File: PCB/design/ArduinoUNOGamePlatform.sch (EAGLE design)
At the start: 23 parts, among them J3 PJ-320D-A, Q1 ON_SEMICONDUCTOR_BC849BLT1GON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, Q2 ON_SEMICONDUCTOR_BC849BLT1GON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

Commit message: Fixed some stale comments and removed commented out old code. Changed some resistor values on PCB following testing. Added designation to move order number under the NES port if using JLC to produce board. Also changed pinouts for buttons to match buttons on shield (I had reversed the positions on PORTC!
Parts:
- R1: value DNP -> 75R
- R2: value 180R -> 220R
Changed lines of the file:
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@@
 <part name="U$2" library="adafruit" library_urn="urn:adsk.eagle:library:21079626" deviceset="ARDUINO" device="-BPLACE" package3d_urn="urn:adsk.eagle:package:21080989/1"/>
 <part name="Q2" library="On Semiconductor - BC849BLT1G" library_urn="urn:adsk.eagle:library:22357129" deviceset="ON_SEMICONDUCTOR_BC849BLT1G" device="ON_SEMICONDUCTOR_BC849BLT1G_0_0" package3d_urn="urn:adsk.eagle:package:22357132/2"/>
-<part name="R2" library="ESP32_DMX_Audio" library_urn="urn:adsk.eagle:library:21091620" deviceset="52101-101-REV-A_RC-MASTER-SMD_R_" device="0603MP" package3d_urn="urn:adsk.eagle:package:21091780/2" value="180R"/>
+<part name="R2" library="ESP32_DMX_Audio" library_urn="urn:adsk.eagle:library:21091620" deviceset="52101-101-REV-A_RC-MASTER-SMD_R_" device="0603MP" package3d_urn="urn:adsk.eagle:package:21091780/2" value="220R"/>
 <part name="R3" library="ESP32_DMX_Audio" library_urn="urn:adsk.eagle:library:21091620" deviceset="52101-101-REV-A_RC-MASTER-SMD_R_" device="0603MP" package3d_urn="urn:adsk.eagle:package:21091780/2" value="1K2"/>
 <part name="R8" library="ESP32_DMX_Audio" library_urn="urn:adsk.eagle:library:21091620" deviceset="52101-101-REV-A_RC-MASTER-SMD_R_" device="0603MP" package3d_urn="urn:adsk.eagle:package:21091780/2" value="470R"/>
@@
 <part name="B8" library="K2-1107ST-A4SW-06" library_urn="urn:adsk.eagle:library:30827574" deviceset="K2-1107ST-A4SW-06" device="" package3d_urn="urn:adsk.eagle:package:30827578/3"/>
 <part name="GND14" library="supply1" library_urn="urn:adsk.eagle:library:371" deviceset="GND" device=""/>
-<part name="R1" library="ESP32_DMX_Audio" library_urn="urn:adsk.eagle:library:21091620" deviceset="52101-101-REV-A_RC-MASTER-SMD_R_" device="0603MP" package3d_urn="urn:adsk.eagle:package:21091780/2" value="DNP"/>
+<part name="R1" library="ESP32_DMX_Audio" library_urn="urn:adsk.eagle:library:21091620" deviceset="52101-101-REV-A_RC-MASTER-SMD_R_" device="0603MP" package3d_urn="urn:adsk.eagle:package:21091780/2" value="75R"/>
 <part name="GND15" library="supply1" library_urn="urn:adsk.eagle:library:371" deviceset="GND" device=""/>
 <part name="U$3" library="PJ-320D-A" library_urn="urn:adsk.eagle:library:43570733" deviceset="NES-CONTROLLER-PORT" device="" package3d_urn="urn:adsk.eagle:package:43570976/2"/>

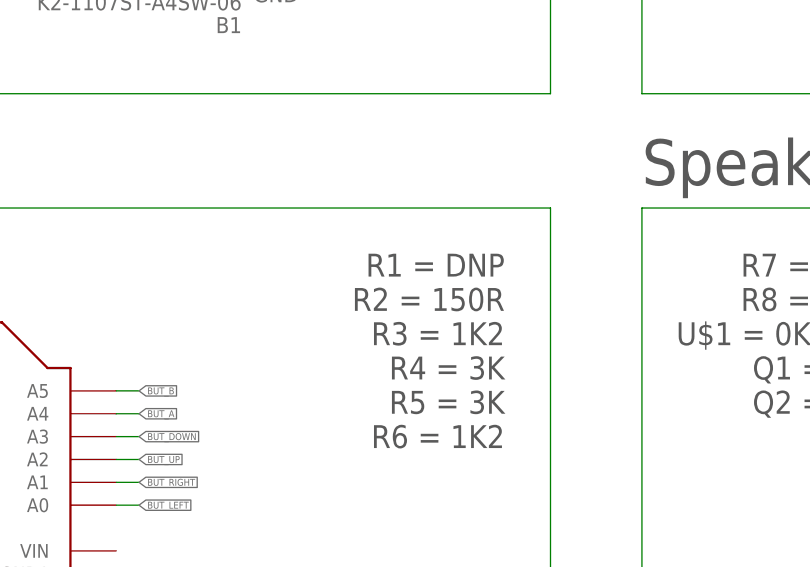
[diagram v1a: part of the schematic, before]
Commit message: Updated schematic to match design files
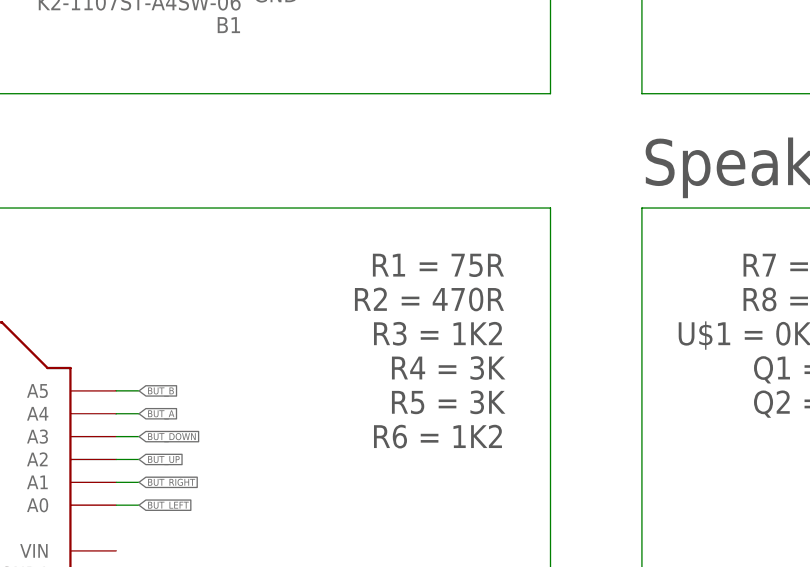
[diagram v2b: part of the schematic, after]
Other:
- note added: "R1 = 75R R2 = 470R R3 = 1K2 R4 = 3K R5 = 3K R6 = 1K2"
- note removed: "R1 = DNP R2 = 150R R3 = 1K2 R4 = 3K R5 = 3K R6 = 1K2"
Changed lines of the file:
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@@
 <text x="256.54" y="205.74" size="5.08" layer="97">NES Controller</text>
 <text x="256.54" y="144.78" size="5.08" layer="97">Speaker output (optional)</text>
-<text x="241.3" y="137.16" size="2.54" layer="97" rot="R180">R1 = DNP
-R2 = 150R
+<text x="241.3" y="137.16" size="2.54" layer="97" rot="R180">R1 = 75R
+R2 = 470R
 R3 = 1K2
 R4 = 3K

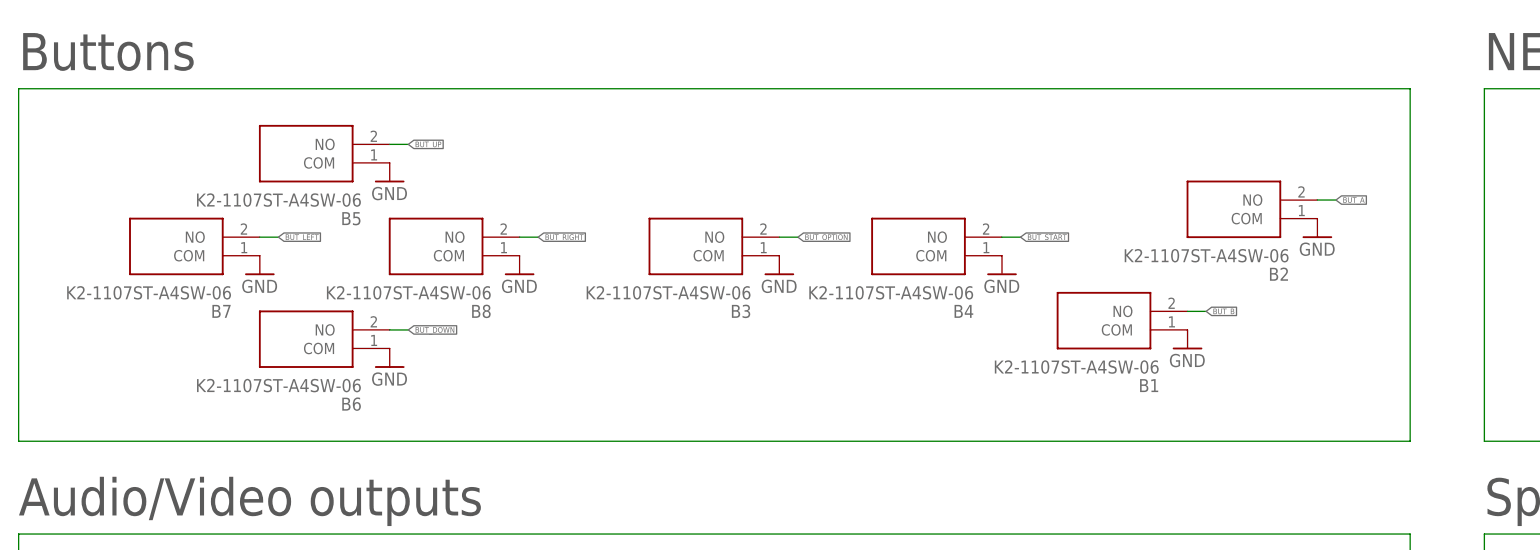
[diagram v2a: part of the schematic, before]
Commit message: Modified PCB design to make it easier for hand-soldering, and also changed to better buttons
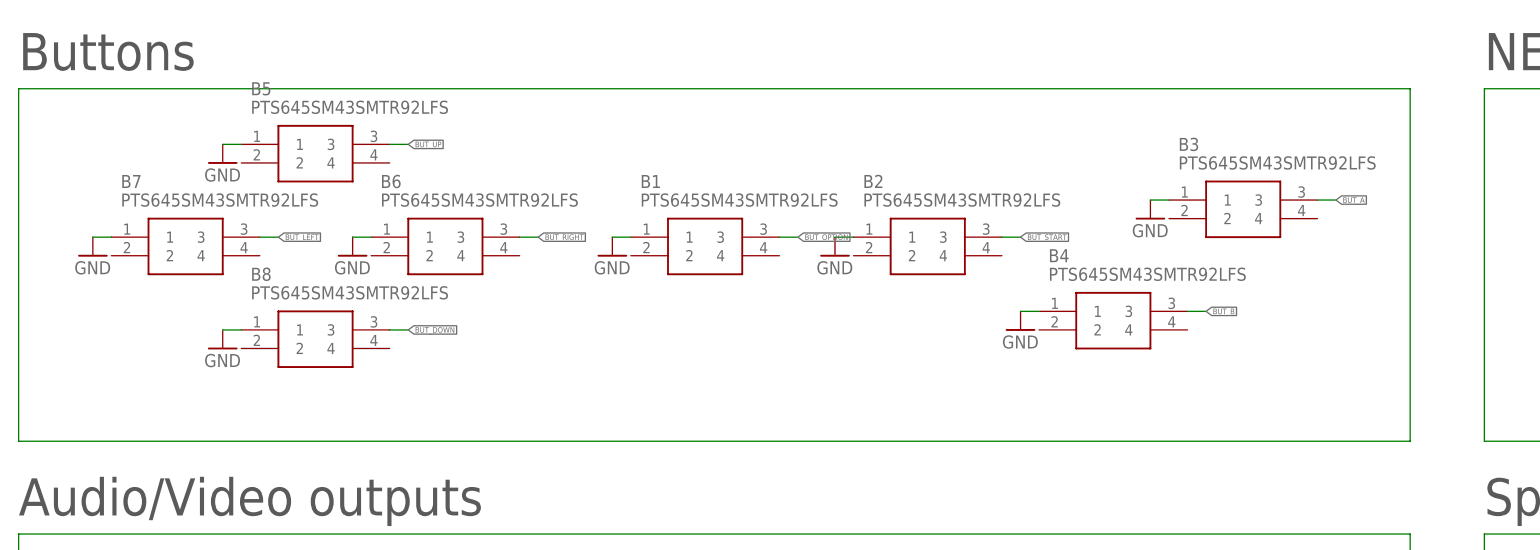
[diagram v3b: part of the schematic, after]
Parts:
- B1, B2, B3, B4, B5, B6, B7, B8: value K2-1107ST-A4SW-06 -> PTS645SM43SMTR92LFS; device K2-1107ST-A4SW-06:K2-1107ST-A4SW-06 -> PTS645SM43SMTR92LFS:PTS645SM43SMTR92LFS
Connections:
- net BUT_A: now also B3.3; no longer B2.NO
- net BUT_B: now also B4.3; no longer B1.NO
- net BUT_DOWN: now also B8.3; no longer B6.NO
- net BUT_LEFT: now also B7.3; no longer B7.NO
- net BUT_OPTION: now also B1.3; no longer B3.NO
- net BUT_RIGHT: now also B6.3; no longer B8.NO
- net BUT_START: now also B2.3; no longer B4.NO
- net BUT_UP: now also B5.3; no longer B5.NO
- net GND: now also B1.1, B2.1, B3.1, B4.1, B5.1, B6.1, B7.1, B8.1; no longer B1.COM, B2.COM, B3.COM, B4.COM, B5.COM, B6.COM, B7.COM, B8.COM

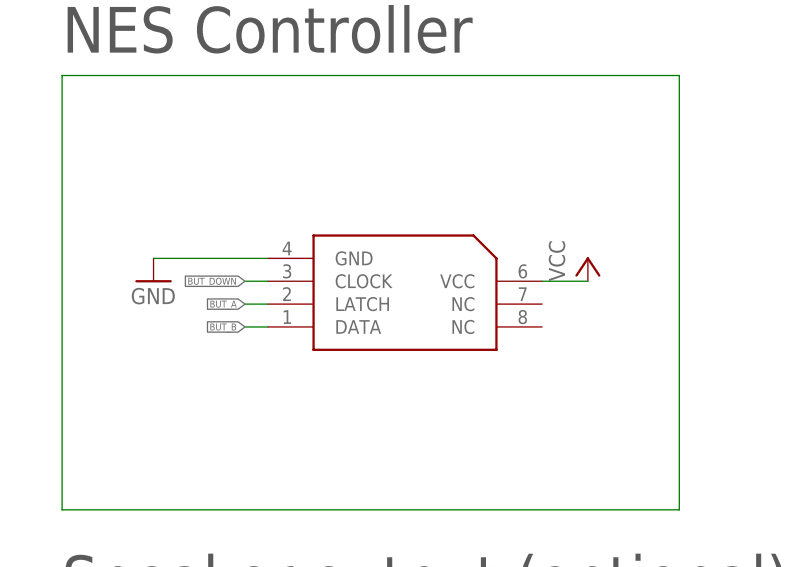
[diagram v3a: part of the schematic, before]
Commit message: Updated PCB design to modify NES port part. Holes were too tight and not enough clearance for it under board, so now on top. Also pins moved slightly further apart to make soldering a little easier
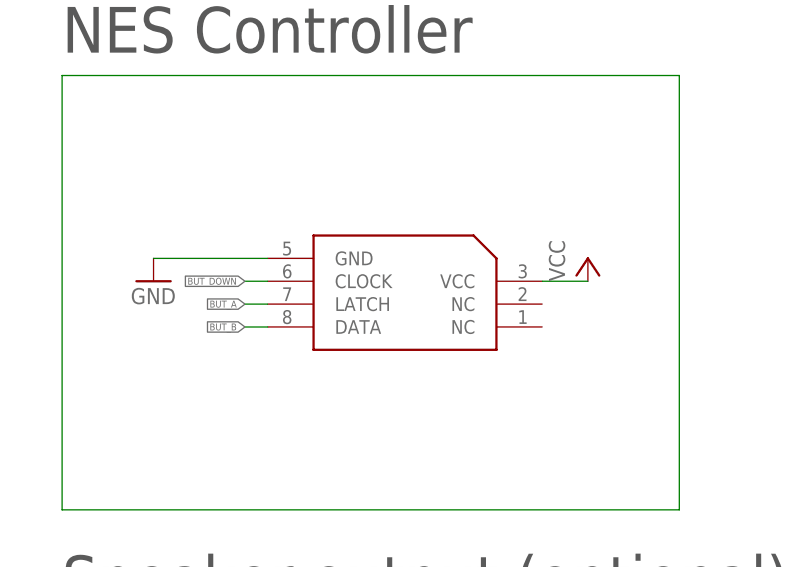
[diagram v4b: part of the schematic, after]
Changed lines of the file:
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@@
 <part name="R1" library="ESP32_DMX_Audio" library_urn="urn:adsk.eagle:library:21091620" deviceset="52101-101-REV-A_RC-MASTER-SMD_R_" device="0603MP" package3d_urn="urn:adsk.eagle:package:21091780/2" value="75R"/>
 <part name="GND15" library="supply1" library_urn="urn:adsk.eagle:library:371" deviceset="GND" device=""/>
-<part name="U$3" library="PJ-320D-A" library_urn="urn:adsk.eagle:library:43570733" deviceset="NES-CONTROLLER-PORT" device="" package3d_urn="urn:adsk.eagle:package:43570976/2"/>
+<part name="U$3" library="PJ-320D-A" library_urn="urn:adsk.eagle:library:43570733" deviceset="NES-CONTROLLER-PORT" device="" package3d_urn="urn:adsk.eagle:package:43570976/3"/>
 <part name="GND16" library="supply1" library_urn="urn:adsk.eagle:library:371" deviceset="GND" device=""/>
 <part name="P+3" library="supply1" library_urn="urn:adsk.eagle:library:371" deviceset="VCC" device=""/>

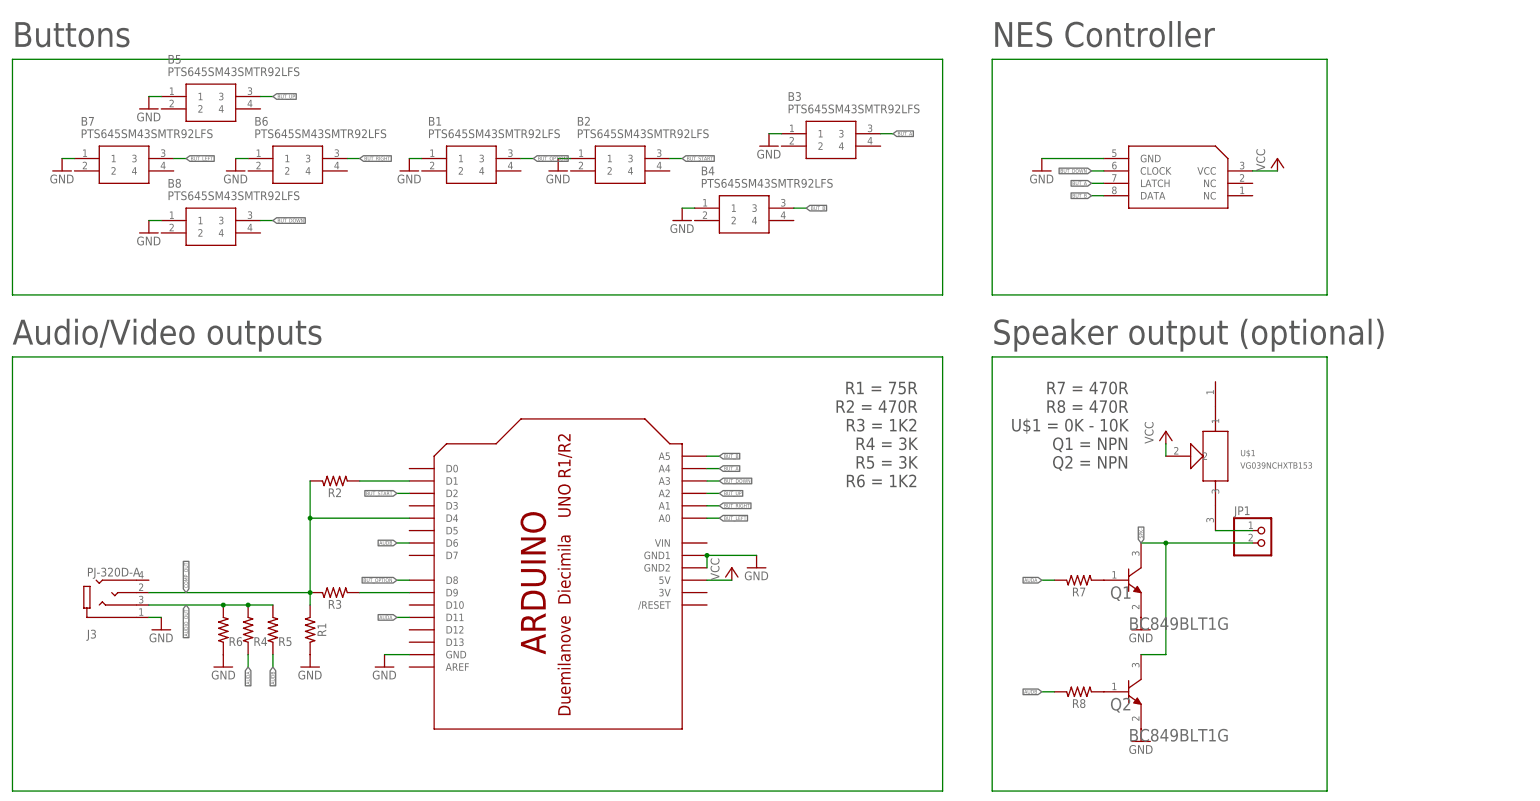
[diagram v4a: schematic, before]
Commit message: Decided to move the pins used for the controller to unused pins on PORTB so that buttons could be used in addition, in future games. Also modified input a little to controller reading. New PCB images and schematic
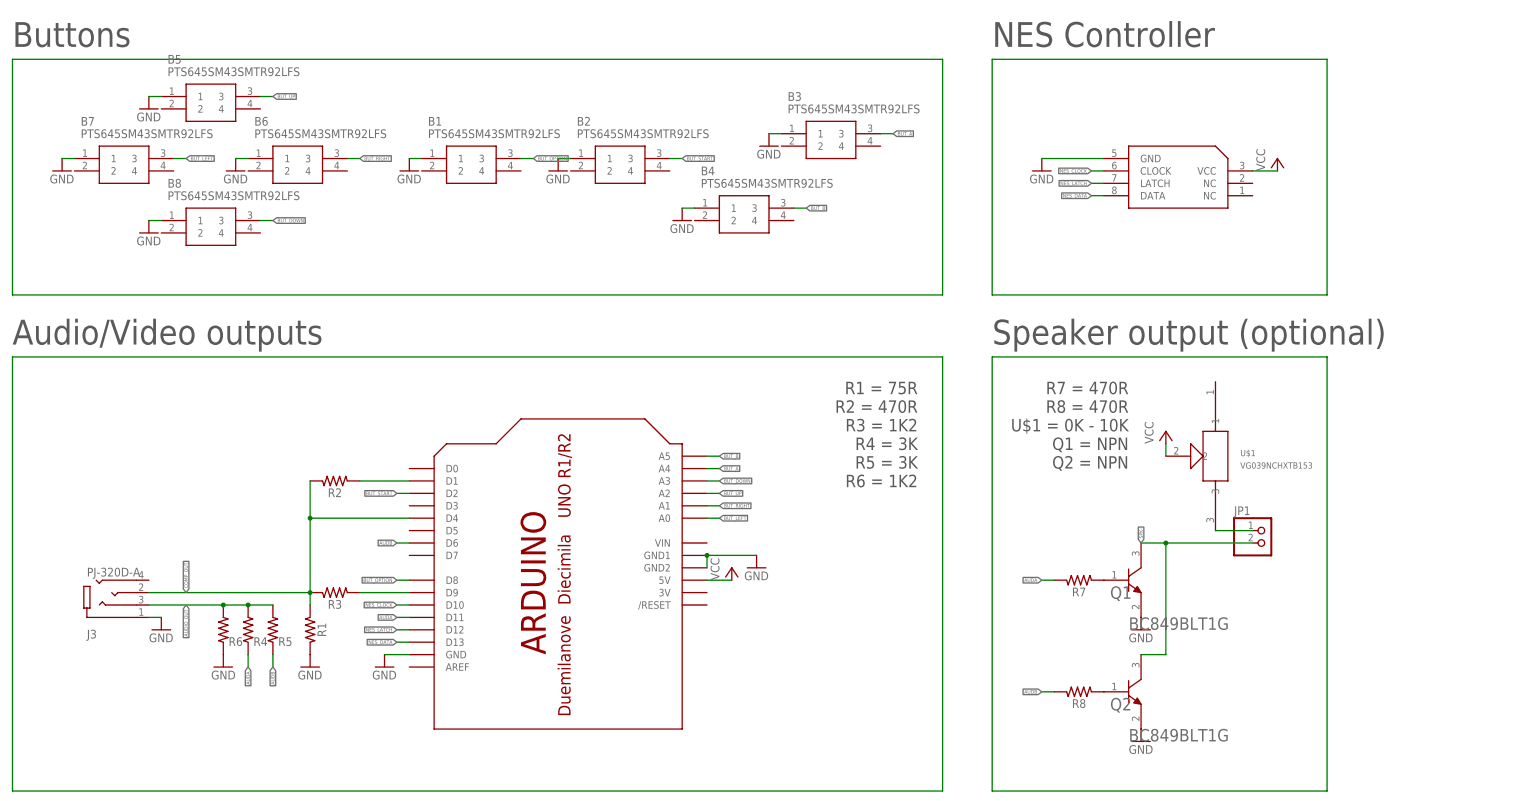
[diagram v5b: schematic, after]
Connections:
- new net NES_CLOCK: U$2.D10, U$3.CLOCK
- new net NES_DATA: U$2.D13, U$3.DATA
- new net NES_LATCH: U$2.D12, U$3.LATCH
- net BUT_A: no longer U$3.LATCH
- net BUT_B: no longer U$3.DATA
- net BUT_DOWN: no longer U$3.CLOCK
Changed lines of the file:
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@@
 <pinref part="B4" gate="G$1" pin="3"/>
-</segment>
-<segment>
-<wire x1="276.86" y1="175.26" x2="279.4" y2="175.26" width="0.1524" layer="91"/>
-<label x="276.86" y="175.26" size="0.762" layer="95" rot="R180" xref="yes"/>
-<pinref part="U$3" gate="G$1" pin="DATA"/>
 </segment>
 </net>
@@
 <pinref part="B3" gate="G$1" pin="3"/>
 </segment>
-<segment>
-<wire x1="276.86" y1="177.8" x2="279.4" y2="177.8" width="0.1524" layer="91"/>
-<label x="276.86" y="177.8" size="0.762" layer="95" rot="R180" xref="yes"/>
-<pinref part="U$3" gate="G$1" pin="LATCH"/>
-</segment>
 </net>
 <net name="BUT_DOWN" class="0">
@@
 <label x="109.22" y="170.18" size="0.762" layer="95" xref="yes"/>
 <pinref part="B8" gate="G$1" pin="3"/>
-</segment>
-<segment>
-<wire x1="276.86" y1="180.34" x2="279.4" y2="180.34" width="0.1524" layer="91"/>
-<label x="276.86" y="180.34" size="0.762" layer="95" rot="R180" xref="yes"/>
-<pinref part="U$3" gate="G$1" pin="CLOCK"/>
 </segment>
 </net>
@@
 </segment>
 </net>
+<net name="NES_DATA" class="0">
+<segment>
+<wire x1="276.86" y1="175.26" x2="279.4" y2="175.26" width="0.1524" layer="91"/>
+<label x="276.86" y="175.26" size="0.762" layer="95" rot="R180" xref="yes"/>
+<pinref part="U$3" gate="G$1" pin="DATA"/>
+</segment>
+<segment>
+<wire x1="134.62" y1="83.82" x2="137.16" y2="83.82" width="0.1524" layer="91"/>
+<label x="134.62" y="83.82" size="0.762" layer="95" rot="R180" xref="yes"/>
+<pinref part="U$2" gate="G$1" pin="D13"/>
+</segment>
+</net>
+<net name="NES_LATCH" class="0">
+<segment>
+<wire x1="134.62" y1="86.36" x2="137.16" y2="86.36" width="0.1524" layer="91"/>
+<label x="134.62" y="86.36" size="0.762" layer="95" rot="R180" xref="yes"/>
+<pinref part="U$2" gate="G$1" pin="D12"/>
+</segment>
+<segment>
+<wire x1="276.86" y1="177.8" x2="279.4" y2="177.8" width="0.1524" layer="91"/>
+<label x="276.86" y="177.8" size="0.762" layer="95" rot="R180" xref="yes"/>
+<pinref part="U$3" gate="G$1" pin="LATCH"/>
+</segment>
+</net>
+<net name="NES_CLOCK" class="0">
+<segment>
+<wire x1="276.86" y1="180.34" x2="279.4" y2="180.34" width="0.1524" layer="91"/>
+<label x="276.86" y="180.34" size="0.762" layer="95" rot="R180" xref="yes"/>
+<pinref part="U$3" gate="G$1" pin="CLOCK"/>
+</segment>
+<segment>
+<wire x1="134.62" y1="91.44" x2="137.16" y2="91.44" width="0.1524" layer="91"/>
+<label x="134.62" y="91.44" size="0.762" layer="95" rot="R180" xref="yes"/>
+<pinref part="U$2" gate="G$1" pin="D10"/>
+</segment>
+</net>
